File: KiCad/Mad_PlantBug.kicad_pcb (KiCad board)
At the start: 2 copper layers, 8 parts, among them IC1 TMP102AIDRLR, Q1 NMOS, U1 YJ-14015, U2 TLV333IDBVR, U3 COMP

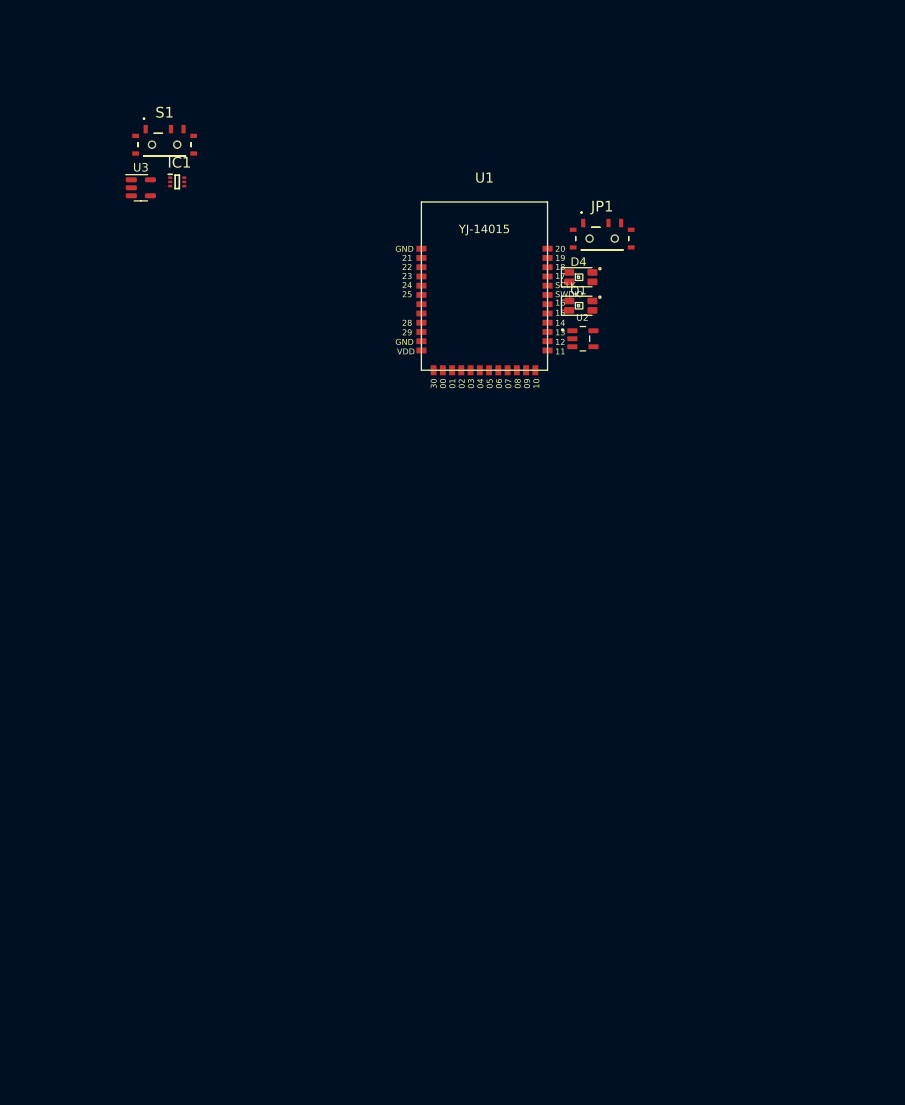
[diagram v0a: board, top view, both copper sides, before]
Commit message: Last version of the full schematics with all assigned footprints. Added simulaion sheet.
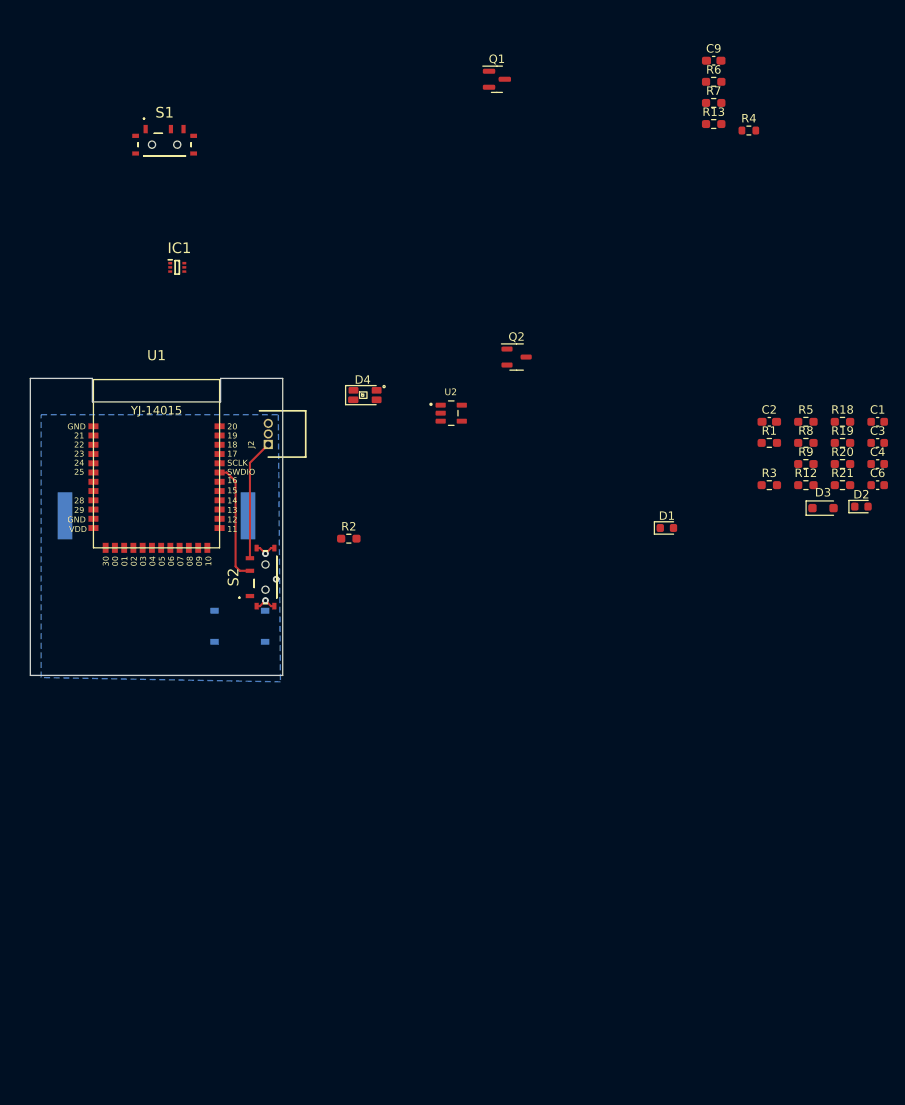
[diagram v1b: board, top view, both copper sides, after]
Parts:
- removed JP1: AUTODISCHARGE, Mad_PlantBug:MSK12C02
- removed U3: COMP, Package_TO_SOT_SMD:SOT-23-5
- added C1: C_Debounce, Capacitor_SMD:C_0603_1608Metric, F.Cu at (148.5, 78.8)
- added C2: C_Dec, Capacitor_SMD:C_0603_1608Metric_Pad1.08x0.95mm_HandSolder, F.Cu at (135.6, 78.8)
- added C3: C_extra, Capacitor_SMD:C_0603_1608Metric, F.Cu at (148.5, 81.3)
- added C4: C_Hold, Capacitor_SMD:C_0603_1608Metric, F.Cu at (148.5, 83.8)
- added C6: C_Dec, Capacitor_SMD:C_0603_1608Metric, F.Cu at (148.5, 86.3)
- added C9: C_Bypass, Capacitor_SMD:C_0603_1608Metric_Pad1.08x0.95mm_HandSolder, F.Cu at (129.0, 35.9)
- added D1: PWR_LED, LED_SMD:LED_0603_1608Metric, F.Cu at (123.4, 91.4)
- added D2: ALIVE_LED, LED_SMD:LED_0603_1608Metric, F.Cu at (146.5, 88.9)
- added D3: 1N5819WS, Mad_PlantBug:D_SOD-323_HandSoldering, F.Cu at (142.0, 89.1)
- added H1: MY-2032-08, Mad_PlantBug:MY203208, B.Cu at (62.7, 90.0)
- added J2: Conn_01x03, Mad_PlantBug:MOLEX_530480310, F.Cu at (76.0, 81.5)
- added Q2: YJL2302B, Mad_PlantBug:SOT-23-3, F.Cu at (105.5, 71.1)
- added R1: R_Pullup, Resistor_SMD:R_0603_1608Metric_Pad0.98x0.95mm_HandSolder, F.Cu at (135.6, 81.3)
- added R12: R_Pulldown, Resistor_SMD:R_0603_1608Metric_Pad0.98x0.95mm_HandSolder, F.Cu at (139.9, 86.3)
- added R13: R_Sense, Resistor_SMD:R_0603_1608Metric_Pad0.98x0.95mm_HandSolder, F.Cu at (129.0, 43.4)
- added R18: R_Pullup, Resistor_SMD:R_0603_1608Metric_Pad0.98x0.95mm_HandSolder, F.Cu at (144.3, 78.8)
- added R19: R_Pullup, Resistor_SMD:R_0603_1608Metric_Pad0.98x0.95mm_HandSolder, F.Cu at (144.3, 81.3)
- added R2: R_Dump, Resistor_SMD:R_0603_1608Metric_Pad0.98x0.95mm_HandSolder, F.Cu at (85.6, 92.7)
- added R20: R_Div, Resistor_SMD:R_0603_1608Metric_Pad0.98x0.95mm_HandSolder, F.Cu at (144.3, 83.8)
- added R21: R_Div, Resistor_SMD:R_0603_1608Metric_Pad0.98x0.95mm_HandSolder, F.Cu at (144.3, 86.3)
- added R3: R_Pulldown, Resistor_SMD:R_0603_1608Metric_Pad0.98x0.95mm_HandSolder, F.Cu at (135.6, 86.3)
- added R4: R_Led, Resistor_SMD:R_0603_1608Metric, F.Cu at (133.2, 44.2)
- added R5: R_Inrush, Resistor_SMD:R_0603_1608Metric_Pad0.98x0.95mm_HandSolder, F.Cu at (139.9, 78.8)
- added R6: R_Discharge, Resistor_SMD:R_0603_1608Metric_Pad0.98x0.95mm_HandSolder, F.Cu at (129.0, 38.4)
- added R7: R_Sense, Resistor_SMD:R_0603_1608Metric_Pad0.98x0.95mm_HandSolder, F.Cu at (129.0, 40.9)
- added R8: R_Pulldown, Resistor_SMD:R_0603_1608Metric_Pad0.98x0.95mm_HandSolder, F.Cu at (139.9, 81.3)
- added R9: R_Inrush, Resistor_SMD:R_0603_1608Metric_Pad0.98x0.95mm_HandSolder, F.Cu at (139.9, 83.8)
- added S2: MSK12C02, Mad_PlantBug:MSK12C02, F.Cu at (75.7, 97.3)
- added S3: PTS526, Mad_PlantBug:PTS526SK15SMTR2LFS, B.Cu at (72.6, 103.1)
- Q1: value NMOS -> AO3401A; footprint Mad_PlantBug:ALS-PDIC15-21BTR8 -> Package_TO_SOT_SMD:SOT-23
- moved U1 44.3 mm to (62.7, 93.8)
- moved D4 29.2 mm to (87.2, 75.7)
- moved Q1 28.6 mm to (103.2, 38.1)
- moved U2 18.0 mm to (97.8, 77.8)
- moved IC1 10.2 mm to (65.2, 60.5)
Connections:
- IC1 pad 1: unconnected-(IC1-SCL-Pad1) -> I2C_SCL
- IC1 pad 2: unconnected-(IC1-GND-Pad2) -> GND
- IC1 pad 4: unconnected-(IC1-ADD0-Pad4) -> GND
- IC1 pad 5: unconnected-(IC1-V+-Pad5) -> VCC
- IC1 pad 6: unconnected-(IC1-SDA-Pad6) -> I2C_SDA
- Q1 pad 1: Net-(D3-A) -> GND
- Q1 pad 2: Net-(Q1-G) -> VCC
- Q1 pad 3: GND -> Net-(Q1-D)
- S1 pad A1: unconnected-(S1-NC-PadA1) -> DISCHARGE_MANUAL
- S1 pad B1: unconnected-(S1-COM-PadB1) -> DISCHARGE
- S1 pad C1: unconnected-(S1-ON-PadC1) -> COMP_OUT
- U1 pad 25: unconnected-(U1-P11-Pad25) -> I2C_SDA
- U1 pad 26: unconnected-(U1-P12-Pad26) -> I2C_SCL
- U2 pad 1: unconnected-(U2-OUT-Pad1) -> COMP_OUT
- U2 pad 2: unconnected-(U2-V--Pad2) -> GND
- U2 pad 3: unconnected-(U2-+IN-Pad3) -> Net-(U2-+IN)
- U2 pad 4: unconnected-(U2--IN-Pad4) -> PWM
- U2 pad 5: unconnected-(U2-V+-Pad5) -> VCC
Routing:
- net SWDIO: track 0.00 -> 14.4 mm
- net SWDIO/nRESET: track 0.00 -> 14.4 mm
- net GND: track 0.00 -> 5.40 mm, vias 0 -> 2
- net Net-(S3-COM_2): vias 0 -> 1
- added copper zone on B.Cu, net GND
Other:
- board outline added: 30 x 35.3 mm
- board text added: "1. Trace 2. Write silkscreen hints for SWD, Battery 3. ERC 4. PCB art"

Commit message: Finished schematics, layed out the components, added ADC battery voltage input, defined board outline, traced a sensor capacitor.
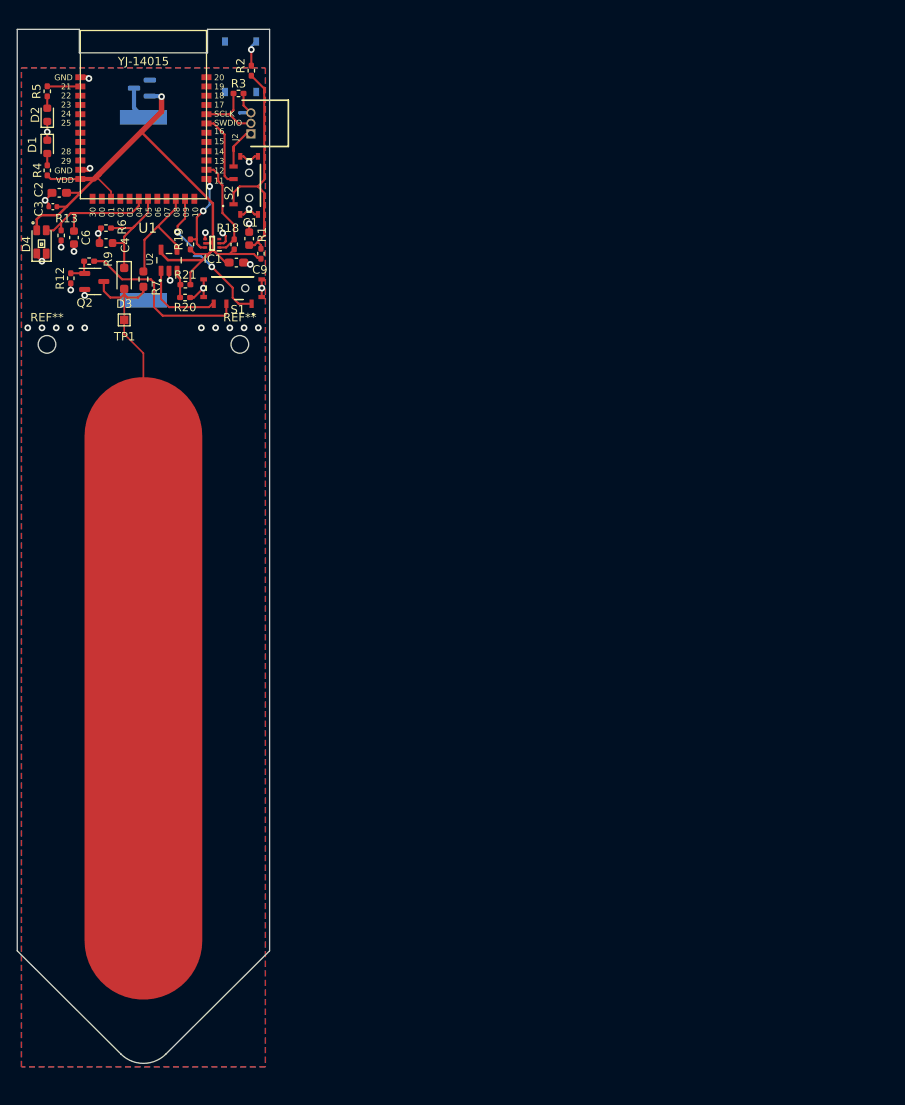
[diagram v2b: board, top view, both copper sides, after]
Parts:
- removed R8: R_Pulldown, Resistor_SMD:R_0603_1608Metric_Pad0.98x0.95mm_HandSolder
- added REF**: MountingHole_2.1mm, MountingHole:MountingHole_2.1mm, F.Cu at (72.6, 69.6)
- added REF**: MountingHole_2.1mm, MountingHole:MountingHole_2.1mm, F.Cu at (49.7, 69.6)
- added TP1: Test_C_Sense, TestPoint:TestPoint_Pad_1.0x1.0mm, F.Cu at (58.9, 66.7)
- C3: footprint Capacitor_SMD:C_0603_1608Metric -> Capacitor_SMD:C_0402_1005Metric
- Q1: moved to B.Cu
- R1, R12, R13, R18, R19, R2, R20, R21, R3, R5, R6, R9: footprint Resistor_SMD:R_0603_1608Metric_Pad0.98x0.95mm_HandSolder -> Resistor_SMD:R_0402_1005Metric_Pad0.72x0.64mm_HandSolder
- R4: footprint Resistor_SMD:R_0603_1608Metric -> Resistor_SMD:R_0402_1005Metric_Pad0.72x0.64mm_HandSolder
- moved D2 107.4 mm to (49.8, 42.3), turned to 90 degrees
- moved C3 102.0 mm to (50.4, 53.2), turned to 180 degrees
- moved C6 100.0 mm to (52.9, 56.9), turned to -90 degrees
- moved R5 98.4 mm to (49.8, 39.5), turned to -90 degrees
- moved C4 95.4 mm to (56.7, 57.6), turned to 180 degrees
- moved R12 90.8 mm to (52.5, 61.8), turned to -90 degrees
- moved C2 88.7 mm to (51.2, 51.6), turned to 180 degrees
- moved R9 88.6 mm to (54.7, 59.7), turned to 180 degrees
- moved D3 87.4 mm to (58.9, 61.8), turned to -90 degrees
- moved D1 86.5 mm to (49.8, 46.1), turned to -90 degrees
- moved R4 83.5 mm to (49.8, 48.9), turned to 90 degrees
- moved R21 81.7 mm to (66.2, 62.5)
- moved R19 81.0 mm to (66.8, 57.7), turned to 90 degrees
- moved R20 80.6 mm to (66.1, 64.0), turned to 180 degrees
- moved R13 78.7 mm to (51.4, 56.7), turned to -90 degrees
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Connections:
- net Net-(D3-A) renamed C_Sense
- C2 pad 1: VCC -> PWR_SENSE
- C3 pad 1: VCC -> PWR_SENSE
- C9 pad 1: VCC -> PWR_SENSE
- D4 pad 1: VCC -> PWR_SENSE
- IC1 pad 5: VCC -> PWR_SENSE
- Q1 pad 2: VCC -> PWR_SENSE
- R1 pad 1: VCC -> PWR_SENSE
- R18 pad 1: VCC -> PWR_SENSE
- R19 pad 1: VCC -> PWR_SENSE
- R21 pad 2: VCC -> PWR_SENSE
- R4 pad 1: VCC -> PWR_SENSE
- U1 pad 12: VCC -> PWR_SENSE
- U1 pad 15: unconnected-(U1-P01-Pad15) -> PWR_SENSE
- U1 pad 2: unconnected-(U1-P21-Pad2) -> SIG_ALIVE
- U1 pad 30: SIG_ALIVE -> unconnected-(U1-P16-Pad30)
- U2 pad 5: VCC -> PWR_SENSE
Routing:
- net C_Sense: track 0.00 -> 83.3 mm
- net PWR_SENSE: track 0.00 -> 80.6 mm, vias 0 -> 1
- net GND: track 5.40 -> 35.2 mm, vias 2 -> 29
- net nRESET: track 0.00 -> 28.6 mm
- net DISCHARGE: track 0.00 -> 21.4 mm
- net DISCHARGE_MANUAL: track 0.00 -> 17.1 mm, vias 0 -> 2
- net LIGHT_SENSE: track 0.00 -> 16.4 mm
- net PWM: track 0.00 -> 14.2 mm
- net CAP_SENSE: track 0.00 -> 13.8 mm
- net I2C_SCL: track 0.00 -> 12.3 mm
- net I2C_SDA: track 0.00 -> 10.9 mm, vias 0 -> 2
- net COMP_OUT: track 0.00 -> 10.3 mm
- net SWDIO: track 14.4 -> 5.53 mm
- net SWCLK: track 0.00 -> 8.40 mm
- net SWDIO/nRESET: track 14.4 -> 8.85 mm
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- added copper zone on F.Cu, net GND
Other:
- board size 30 x 35.3 mm -> 30 x 122.9 mm
- board text added: "1. Trace 2. Write silkscreen hints for SWD, Battery 3. ERC 4. PCB art 5. Board outline ears 6. Generate BOM"
- board text removed: "1. Trace 2. Write silkscreen hints for SWD, Battery 3. ERC 4. PCB art"

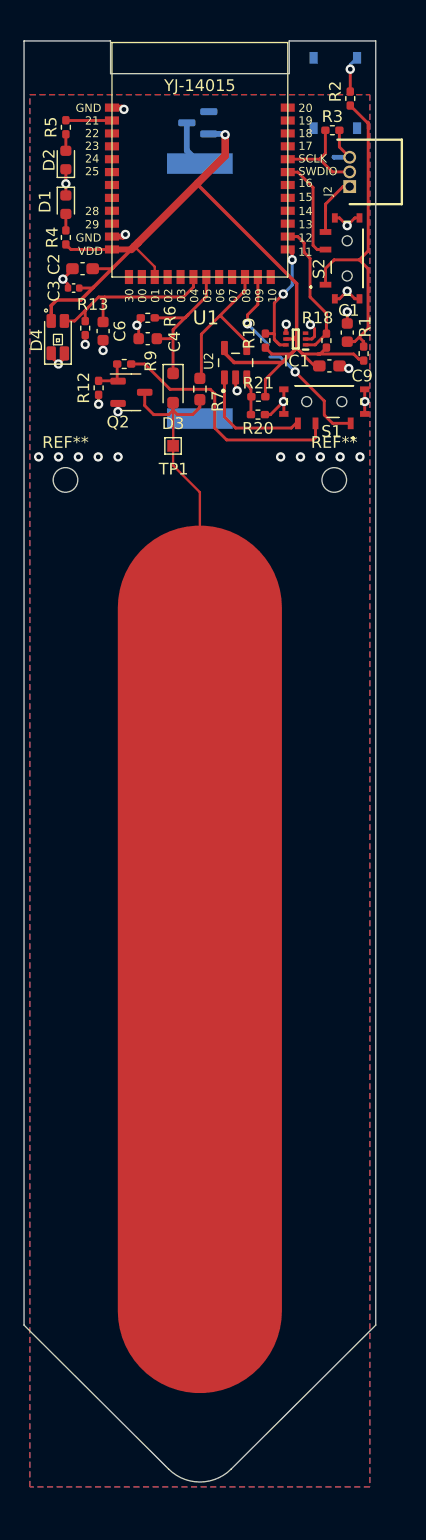
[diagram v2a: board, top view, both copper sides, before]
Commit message: First version of the sensor is up.
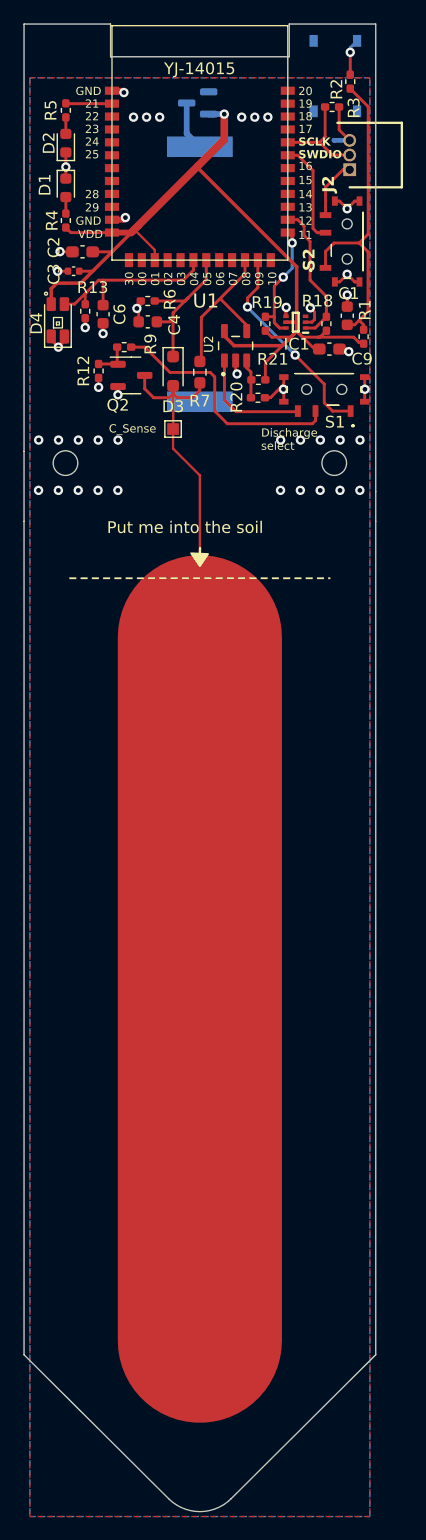
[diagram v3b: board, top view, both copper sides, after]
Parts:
- added G***: LOGO, Mad_PlantBug:brain_logo, B.Cu at (60.8, 77.2)
- moved R3 1.98 mm to (72.5, 37.8)
- moved Q1 1.69 mm to (61.0, 37.5)
- moved C1 1.44 mm to (73.8, 55.6)
- moved C2 1.44 mm to (51.2, 50.2)
- moved C4 1.44 mm to (56.7, 56.1)
- moved D1 1.44 mm to (49.8, 44.7)
- moved IC1 1.44 mm to (69.4, 56.2)
- moved R13 1.44 mm to (51.4, 55.2)
- moved R20 1.44 mm to (66.1, 62.6)
- moved R7 1.44 mm to (61.2, 60.4)
- moved R9 1.44 mm to (54.7, 58.3)
- moved REF** 1.44 mm to (72.6, 68.2)
- moved REF** 1.44 mm to (49.7, 68.2)
- moved C3 1.44 mm to (50.4, 51.8)
- moved C6 1.44 mm to (52.9, 55.5)
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- renumbered TP1 to C_Sense
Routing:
- net C_Sense: track 83.3 -> 90.6 mm
- net DISCHARGE_MANUAL: track 17.1 -> 18.1 mm
- net SWCLK: track 8.40 -> 9.00 mm
- net nRESET: track 28.6 -> 28.0 mm
- net GND: track 35.2 -> 35.6 mm, vias 29 -> 46
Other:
- board size 30 x 122.9 mm -> 30 x 126.9 mm
- board text added: "Discharge select"
- board text added: "Line markers for easy rescaling"
- board text added: "Mad_PlantBug v1.0"
- board text added: "Put me into the soil"
- board text added: "SWCLK"
- board text added: "SWD/nRST select"
- board text added: "SWDIO"
- board text added: "nRST"
- board text removed: "1. Trace 2. Write silkscreen hints for SWD, Battery 3. ERC 4. PCB art 5. Board outline ears 6. Generate BOM"
